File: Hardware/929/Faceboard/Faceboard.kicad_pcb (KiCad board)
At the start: 4 copper layers, 154 x 144 mm, 94 parts, among them J2 Raspberry_Pi_to_Ziloo, J3 Debug_4-2328724-5, P1 UCM-P1, P2 UCM-P2, P5 T-USB_PWRCTL-50, P6 T-USB_HIGH-SPEED-50, P7 202-SMART-CAM, Q1 2SC4213, U10 CBTL04083ABS_518, U11 TS5USBC410YFFR, U12 FR2032, U16 TXS0104, U16 YZT12, U17 TXS0104, U17 YZT12, U18 SN74CB3Q3245RGYR, U19 TXS0104, U20 TXS0104, U21 TXS0104, U3 SN74CB3Q3245RGYR, U6 Supervisor M2, U7 TCA9534, Y1 25.000MHz

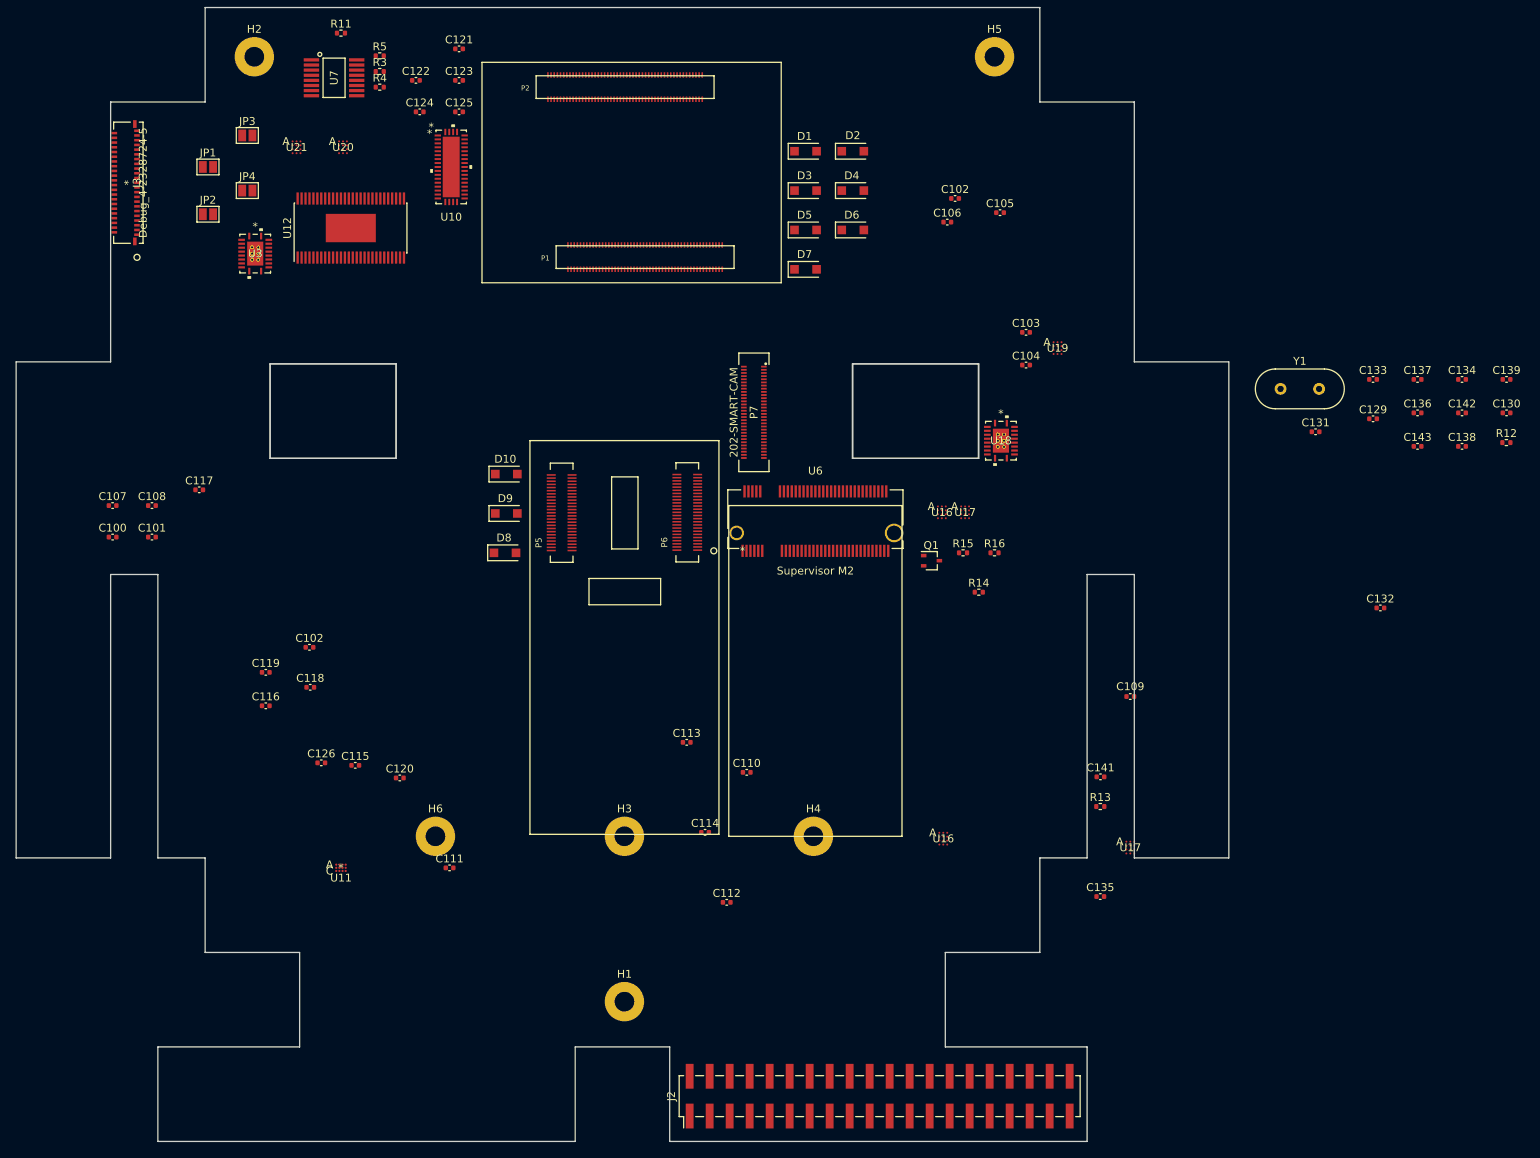
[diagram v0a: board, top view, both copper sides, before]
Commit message: Added components
ESD HDMI
Extra components planned
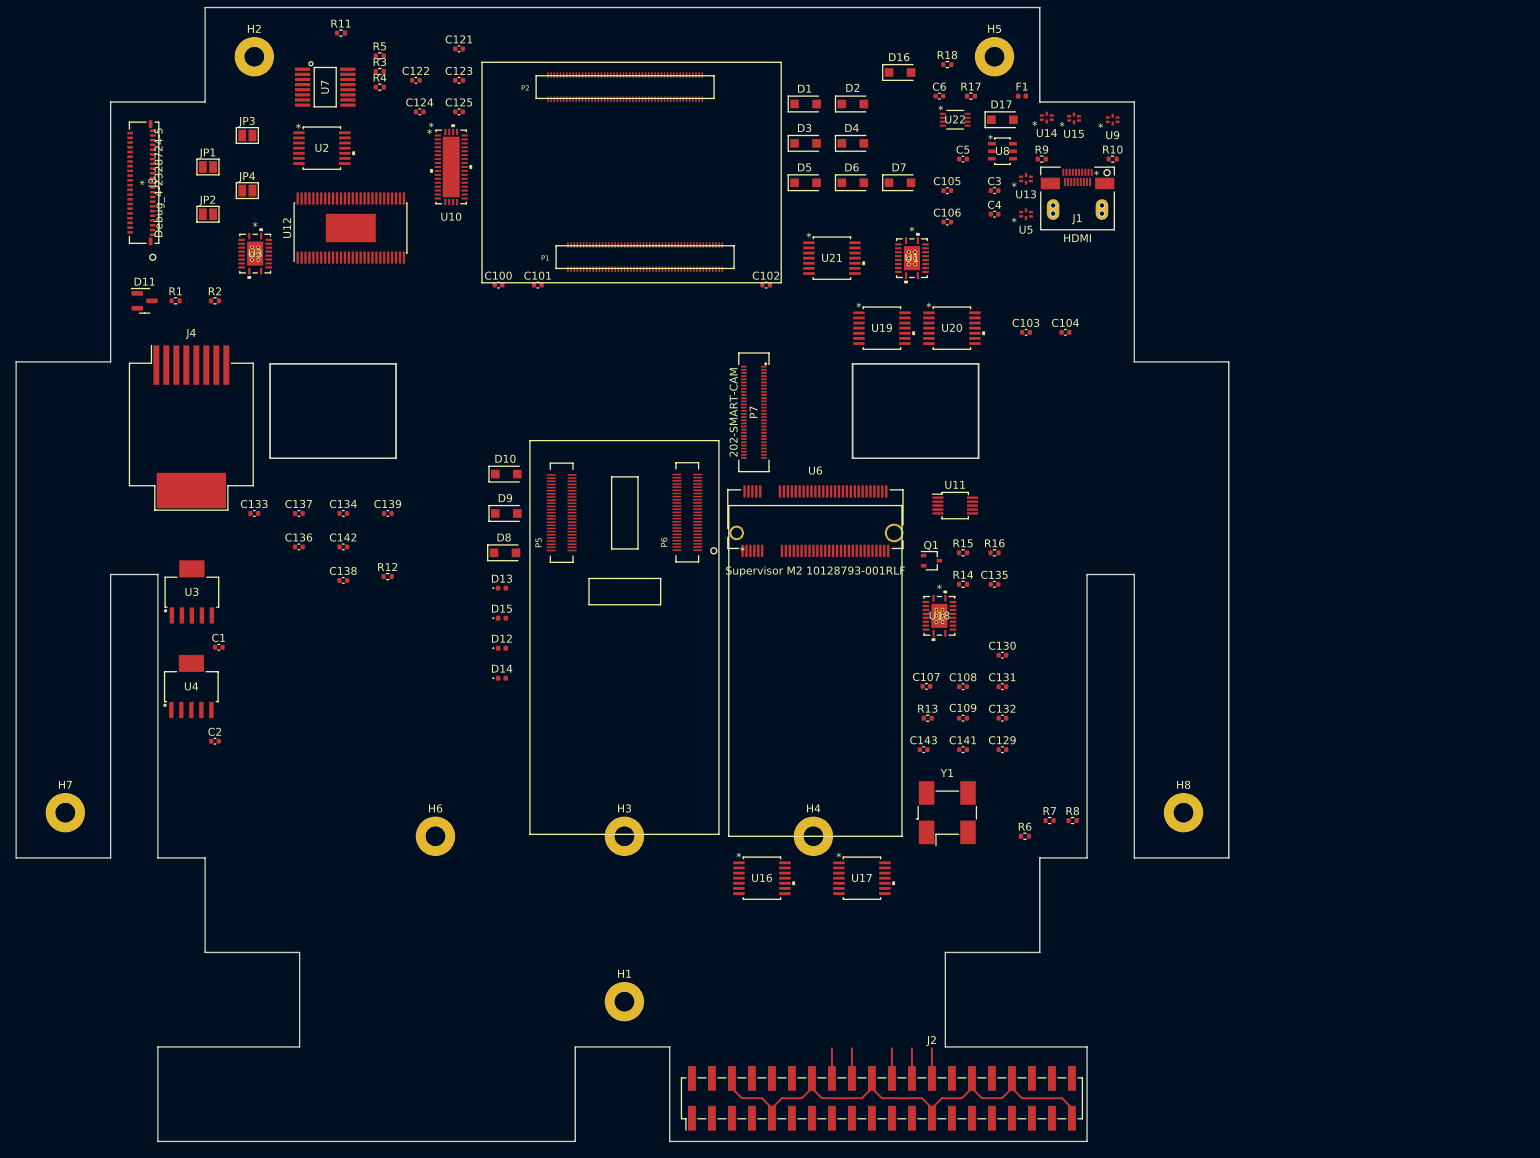
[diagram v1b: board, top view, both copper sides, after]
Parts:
- removed the C102 at (149.2, 61.2)
- removed C110, C111, C112, C113, C114, C115, C117, C118, C119, C120: 100nF, Capacitor_SMD:C_0402_1005Metric
- removed C116: 1uF, Capacitor_SMD:C_0402_1005Metric
- removed C126: CAP, Capacitor_SMD:C_0402_1005Metric
- removed the U16 at (147.7, 142.5)
- removed the U16 at (147.6, 101.1)
- removed the U17 at (150.5, 101.1)
- removed the U17 at (171.5, 143.7)
- added C1: C, Capacitor_SMD:C_0402_1005Metric, F.Cu at (55.7, 118.2)
- added C2: C, Capacitor_SMD:C_0402_1005Metric, F.Cu at (55.2, 130.2)
- added C3: 1uF, Capacitor_SMD:C_0402_1005Metric, F.Cu at (154.2, 60.2)
- added C4: 1uF, Capacitor_SMD:C_0402_1005Metric, F.Cu at (154.2, 63.2)
- added C5: 1uF, Capacitor_SMD:C_0402_1005Metric, F.Cu at (150.2, 56.2)
- added C6: 10nF, Capacitor_SMD:C_0402_1005Metric, F.Cu at (147.2, 48.2)
- added D11: BAT54C, Package_TO_SOT_SMD:SOT-23, F.Cu at (46.3, 74.2)
- added D12: D, Diode_SMD:D_0402_1005Metric, F.Cu at (91.7, 118.4)
- added D13: D, Diode_SMD:D_0402_1005Metric, F.Cu at (91.7, 110.7)
- added D14: D, Diode_SMD:D_0402_1005Metric, F.Cu at (91.7, 122.2)
- added D15: D, Diode_SMD:D_0402_1005Metric, F.Cu at (91.7, 114.5)
- added D16: 1A Schottky, Diode_SMD:D_SOD-123F, F.Cu at (142.2, 45.2)
- added D17: 1A Schottky, Diode_SMD:D_SOD-123F, F.Cu at (155.2, 51.2)
- added F1: Polyfuse_Small, Fuse:Fuse_0402_1005Metric, F.Cu at (157.7, 48.2)
- added H7: MountingHole, MountingHole:MountingHole_2.5mm_Pad, F.Cu at (36.2, 139.2)
- added H8: MountingHole, MountingHole:MountingHole_2.5mm_Pad, F.Cu at (178.2, 139.2)
- added J1: HDMI, Ziloo:467652301, F.Cu at (164.8, 61.2)
- added J4: RJ45_LED_Shielded, Connector_RJ:RJ45_Molex_0855135013_Vertical, F.Cu at (52.2, 90.2)
- added R1: 475Ohm, Resistor_SMD:R_0402_1005Metric, F.Cu at (50.2, 74.2)
- added R10: 1K2, Resistor_SMD:R_0402_1005Metric, F.Cu at (169.2, 56.2)
- added R17: 1K/1%, Resistor_SMD:R_0402_1005Metric, F.Cu at (151.2, 48.2)
- added R18: 200K, Resistor_SMD:R_0402_1005Metric, F.Cu at (148.2, 44.2)
- added R2: 475Ohm, Resistor_SMD:R_0402_1005Metric, F.Cu at (55.2, 74.2)
- added R6: 2M, Resistor_SMD:R_0402_1005Metric, F.Cu at (158.1, 142.2)
- added R7: 1M, Resistor_SMD:R_0402_1005Metric, F.Cu at (161.2, 140.2)
- added R8: 1K, Resistor_SMD:R_0402_1005Metric, F.Cu at (164.2, 140.2)
- added R9: 47K, Resistor_SMD:R_0402_1005Metric, F.Cu at (160.2, 56.2)
- added U1: SN74CB3Q3245RGYR, Ziloo:SN74CB3Q3245RGYR, F.Cu at (143.8, 68.8)
- added U13: LCFE121002H900TG, Ziloo:LCFE121002H900TG, F.Cu at (158.2, 58.8)
- added U14: LCFE121002H900TG, Ziloo:LCFE121002H900TG, F.Cu at (160.9, 51.0)
- added U15: LCFE121002H900TG, Ziloo:LCFE121002H900TG, F.Cu at (164.3, 51.1)
- added U16: TXS0104EPWR, Ziloo:TXS0104EPWR, F.Cu at (124.7, 147.6)
- added U17: TXS0104EPWR, Ziloo:TXS0104EPWR, F.Cu at (137.4, 147.6)
- added U2: SN74CBTLV3126PWR, Ziloo:SN74CBTLV3126PWR, F.Cu at (68.8, 54.9)
- added U22: PCA9306DCUR, Ziloo:PCA9306DCUR, F.Cu at (149.2, 51.2)
- added U3: TPS79633DCQ, Ziloo:TPS79633DCQ, F.Cu at (52.3, 111.2)
- added U4: TPS79618DCQR, Ziloo:TPS79618DCQR, F.Cu at (52.2, 123.2)
- added U5: LCFE121002H900TG, Ziloo:LCFE121002H900TG, F.Cu at (158.2, 63.2)
- added U8: IP4220CZ6, Ziloo:IP4220CZ6, F.Cu at (155.2, 55.2)
- added U9: LCFE121002H900TG, Ziloo:LCFE121002H900TG, F.Cu at (169.2, 51.2)
- P5: value T-USB_PWRCTL-50 -> 292_PWRCTL-50
- P6: value T-USB_HIGH-SPEED-50 -> 292_HIGH-SPEED-50
- U11: value TS5USBC410YFFR -> FSUSB42MUX; footprint Ziloo:TS5USBC410YFFR -> Package_SO:MSOP-10_3x3mm_P0.5mm
- U12: value FR2032 -> Faceboard_Expander_FR2032IG56
- U19, U20, U21: value TXS0104 -> TXS0104EPWR; footprint Ziloo:TXS0104EYZTR -> Ziloo:TXS0104EPWR
- U6: value Supervisor M2 -> Supervisor M2 10128793-001RLF
- Y1: footprint Crystal:Crystal_HC18-U_Vertical -> Oscillator:Oscillator_SMD_Abracon_ASV-4Pin_7.0x5.1mm_HandSoldering
- moved C133 143.1 mm to (60.2, 101.2)
- moved C134 143.1 mm to (71.5, 101.2)
- moved C136 143.1 mm to (65.9, 105.5)
- moved C137 143.1 mm to (65.9, 101.2)
- moved C138 143.1 mm to (71.5, 109.8)
- moved C139 143.1 mm to (77.2, 101.2)
- moved C142 143.1 mm to (71.5, 105.5)
- moved R12 143.1 mm to (77.2, 109.3)
- moved C107 105.9 mm to (145.6, 123.2)
- moved C108 105.5 mm to (150.2, 123.2)
- moved U11 90.6 mm to (149.2, 100.2)
- moved U20 80.7 mm to (148.8, 77.7)
- moved C102 74.0 mm to (125.2, 72.2)
- moved C143 73.6 mm to (145.2, 131.2)
- moved C130 71.0 mm to (155.2, 119.2)
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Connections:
- net /Expander, M.2 and T-USB/M.2 Key B connector/B_PWROFF renamed Net-(R13-Pad1)
- net /Expander, M.2 and T-USB/SPI2_SS0 renamed /Expander, M.2 and T-USB/POWER_TO_SYS_STEM
- net /UART1_TXD renamed /C_EX_RXD
- net Net-(D6-Pad2) renamed /Expander, M.2 and T-USB/VSOM
- C103 pad 1: +1V8 -> SLEEP_1V8
- C104 pad 1: +3.3V -> CAM_3V3
- C105 pad 1: +1V8 -> SLEEP_1V8
- C106 pad 1: +3.3V -> CAM_3V3
- C107 pad 1: +1V8 -> SLEEP_1V8
- C108 pad 1: +3.3V -> CAM_3V3
- C121 pad 2: +3.3V -> LIVE_3V3
- C122 pad 2: +3.3V -> LIVE_3V3
- C123 pad 2: +3.3V -> LIVE_3V3
- C124 pad 2: +3.3V -> LIVE_3V3
- C125 pad 2: +3.3V -> LIVE_3V3
- C130 pad 1: +3.3V -> LIVE_3V3
- C131 pad 1: +3.3V -> LIVE_3V3
- C132 pad 1: +3.3V -> LIVE_3V3
- C133 pad 1: +1V8 -> LIVE_1V8
- C134 pad 1: +3.3V -> LIVE_3V3
- C136 pad 1: +3.3V -> LIVE_3V3
- C137 pad 1: +3.3V -> LIVE_3V3
- C138 pad 1: +3.3V -> LIVE_3V3
- C139 pad 1: +3.3V -> LIVE_3V3
- C141 pad 1: +1V8 -> LIVE_1V8
- C142 pad 1: +3.3V -> LIVE_3V3
- D8 pad 2: Net-(D8-Pad2) -> Net-(P5-Pad15)
- J2 pad 1: unconnected-(J2-Pad1) -> LIVE_3V3
- J2 pad 13: unconnected-(J2-Pad13) -> /Ethernet and SD1/SD1_DATA3
- J2 pad 14: unconnected-(J2-Pad14) -> GND
- J2 pad 15: unconnected-(J2-Pad15) -> /Ethernet and SD1/SD1_CLK
- J2 pad 16: unconnected-(J2-Pad16) -> /Ethernet and SD1/SD1_CMD
- J2 pad 17: unconnected-(J2-Pad17) -> LIVE_3V3
- J2 pad 18: unconnected-(J2-Pad18) -> /Ethernet and SD1/SD1_DATA0
- J2 pad 2: unconnected-(J2-Pad2) -> HDMI_5V
- J2 pad 20: unconnected-(J2-Pad20) -> GND
- J2 pad 22: unconnected-(J2-Pad22) -> /Ethernet and SD1/SD1_DATA1
- J2 pad 25: unconnected-(J2-Pad25) -> GND
- J2 pad 27: unconnected-(J2-Pad27) -> /Ethernet and SD1/SYS_I2C_SDA
- J2 pad 28: unconnected-(J2-Pad28) -> /Ethernet and SD1/SYS_I2C_SCL
- J2 pad 3: unconnected-(J2-Pad3) -> /Ethernet and SD1/STEM_I2C_SDA
- J2 pad 30: unconnected-(J2-Pad30) -> GND
- J2 pad 34: unconnected-(J2-Pad34) -> GND
- J2 pad 37: unconnected-(J2-Pad37) -> /Ethernet and SD1/SD1_DATA2
- J2 pad 39: unconnected-(J2-Pad39) -> GND
- J2 pad 4: unconnected-(J2-Pad4) -> HDMI_5V
- J2 pad 5: unconnected-(J2-Pad5) -> /Ethernet and SD1/STEM_I2C_SCL
- J2 pad 6: unconnected-(J2-Pad6) -> GND
- J2 pad 7: unconnected-(J2-Pad7) -> /Ethernet and SD1/STEM_INT
- J2 pad 9: unconnected-(J2-Pad9) -> GND
- J3 pad 14: unconnected-(J3-Pad14) -> /Expander, M.2 and T-USB/SJTAG_MOD
- J3 pad 2: +3.3V -> CAM_3V3
- J3 pad 24: unconnected-(J3-Pad24) -> Net-(J3-Pad24)
- J3 pad 25: unconnected-(J3-Pad25) -> Net-(J3-Pad25)
- J3 pad 26: unconnected-(J3-Pad26) -> Net-(J3-Pad26)
- J3 pad 27: unconnected-(J3-Pad27) -> Net-(J3-Pad27)
- J3 pad 28: unconnected-(J3-Pad28) -> Net-(J3-Pad28)
- J3 pad 29: unconnected-(J3-Pad29) -> Net-(J3-Pad29)
- J3 pad 5: unconnected-(J3-Pad5) -> /Expander, M.2 and T-USB/UART2_RXD
- J3 pad 6: unconnected-(J3-Pad6) -> /Expander, M.2 and T-USB/UART2_RXD
- J3 pad 8: unconnected-(J3-Pad8) -> /Expander, M.2 and T-USB/UART4_RXD
- J3 pad 9: unconnected-(J3-Pad9) -> /Expander, M.2 and T-USB/UART4_TXD
- JP2 pad 1: unconnected-(JP2-Pad1) -> /Expander, M.2 and T-USB/SYS_PD_CTL_INT
- JP3 pad 1: /Expander, M.2 and T-USB/SYS_I2C_SDA -> /Expander, M.2 and T-USB/POWER_PD_CTL_INT
- JP4 pad 1: /Expander, M.2 and T-USB/SYS_I2C_SCL -> /Expander, M.2 and T-USB/BAT_INT
- P1 pad 87: /NIGHT_I2C_SCL -> /I2C6_SCL
- P1 pad 89: /NIGHT_I2C_SDA -> /I2C6_SDA
- P5 pad 10: unconnected-(P5-Pad10) -> Net-(J3-Pad29)
- P5 pad 11: /Expander, M.2 and T-USB/BOTH_VSOM -> GND
- P5 pad 15: Net-(D8-Pad2) -> Net-(P5-Pad15)
- P5 pad 16: /Expander, M.2 and T-USB/SYS_RST_PMIC -> /Expander, M.2 and T-USB/USB_XD_OE
- P5 pad 17: /Expander, M.2 and T-USB/POR_B_3P3 -> /Expander, M.2 and T-USB/USB_XD_SEL
- P5 pad 20: /Expander, M.2 and T-USB/VCC_RTC -> /Expander, M.2 and T-USB/ALT_BOOT
- P5 pad 22: /Expander, M.2 and T-USB/ALT_BOOT -> unconnected-(P5-Pad22)
- P5 pad 23: unconnected-(P5-Pad23) -> /Expander, M.2 and T-USB/BAT_INT
- P5 pad 24: unconnected-(P5-Pad24) -> /Expander, M.2 and T-USB/BAT_CE
- P5 pad 25: unconnected-(P5-Pad25) -> /Expander, M.2 and T-USB/BAT_EN
- P5 pad 27: unconnected-(P5-Pad27) -> /Expander, M.2 and T-USB/SHUTDOWN_BTN
- P5 pad 28: unconnected-(P5-Pad28) -> /Expander, M.2 and T-USB/LOCK_BTN
- P5 pad 35: /Expander, M.2 and T-USB/NIGHT_I2C_SDA -> /Expander, M.2 and T-USB/POWER_SDA
- P5 pad 36: /Expander, M.2 and T-USB/NIGHT_I2C_SCL -> /Expander, M.2 and T-USB/POWER_SCL
- P5 pad 40: unconnected-(P5-Pad40) -> CAM_3V3
- P5 pad 41: /Expander, M.2 and T-USB/UART4_TXD -> unconnected-(P5-Pad41)
- P5 pad 42: /Expander, M.2 and T-USB/UART4_RXD -> unconnected-(P5-Pad42)
- P5 pad 43: /Expander, M.2 and T-USB/UART3_RXD -> CAM_3V3
- P5 pad 44: /Expander, M.2 and T-USB/UART3_TXD -> Net-(J3-Pad27)
- P5 pad 45: /Expander, M.2 and T-USB/UART2_RXD -> Net-(J3-Pad26)
- P5 pad 46: /Expander, M.2 and T-USB/UART2_RXD -> HDMI_5V
- P5 pad 47: /Expander, M.2 and T-USB/FACE-EX_FW_RXD -> Net-(J3-Pad25)
- P5 pad 48: /Expander, M.2 and T-USB/UART1_TXD -> Net-(J3-Pad24)
- P5 pad 49: GND -> /Expander, M.2 and T-USB/VCC_RTC
- P5 pad 9: unconnected-(P5-Pad9) -> Net-(J3-Pad28)
- P6 pad 19: /Expander, M.2 and T-USB/FACE-EX_FW_TXD -> /Expander, M.2 and T-USB/STEM_INT
- P6 pad 21: /Expander, M.2 and T-USB/T_SBWTCK -> unconnected-(P6-Pad21)
- P6 pad 23: /Expander, M.2 and T-USB/T_SBWTDIO -> unconnected-(P6-Pad23)
- P6 pad 27: /Expander, M.2 and T-USB/T-USB-EX_FW_TXD -> unconnected-(P6-Pad27)
- P6 pad 28: /Expander, M.2 and T-USB/T-USB-EX_FW_RXD -> unconnected-(P6-Pad28)
- P6 pad 30: unconnected-(P6-Pad30) -> /Expander, M.2 and T-USB/PWR_CHARGE
- P7 pad 12: +1V8 -> SLEEP_1V8
- P7 pad 24: +3.3V -> CAM_3V3
- P7 pad 30: +1V8 -> SLEEP_1V8
- P7 pad 35: unconnected-(P7-Pad35) -> /Camera + Sound Domain/C_FW_TXD
- P7 pad 37: unconnected-(P7-Pad37) -> /Camera + Sound Domain/C_FW_RXD
- P7 pad 47: unconnected-(P7-Pad47) -> /Camera + Sound Domain/SD_CS_SOM
- P7 pad 49: unconnected-(P7-Pad49) -> /Camera + Sound Domain/SD_D3
- P7 pad 51: unconnected-(P7-Pad51) -> /Camera + Sound Domain/SD_D2
- P7 pad 53: unconnected-(P7-Pad53) -> /Camera + Sound Domain/SD_D1
- P7 pad 55: unconnected-(P7-Pad55) -> /Camera + Sound Domain/SD_D0
- P7 pad 57: unconnected-(P7-Pad57) -> /Camera + Sound Domain/SD_CLK
- P7 pad 59: unconnected-(P7-Pad59) -> /Camera + Sound Domain/SD_CMD
- P7 pad 6: +3.3V -> CAM_3V3
- R11 pad 1: +3.3V -> LIVE_3V3
- R12 pad 2: +3.3V -> LIVE_3V3
- R13 pad 2: +3.3V -> LIVE_3V3
- R14 pad 1: +3.3V -> LIVE_3V3
- R3 pad 1: +3.3V -> LIVE_3V3
- R4 pad 1: Net-(R4-Pad1) -> Net-(U7-Pad1)
- R5 pad 1: +3.3V -> LIVE_3V3
- R5 pad 2: Net-(R5-Pad2) -> Net-(U7-Pad2)
- U10 pad 13: +3.3V -> LIVE_3V3
- U10 pad 18: +3.3V -> LIVE_3V3
- U10 pad 20: +3.3V -> LIVE_3V3
- U10 pad 30: +3.3V -> LIVE_3V3
- U10 pad 40: +3.3V -> LIVE_3V3
- U10 pad 42: +3.3V -> LIVE_3V3
- U10 pad 5: +3.3V -> LIVE_3V3
- U10 pad 8: +3.3V -> LIVE_3V3
- U12 pad 12: unconnected-(U12-Pad12) -> /Expander, M.2 and T-USB/STEM_INT
- U12 pad 13: unconnected-(U12-Pad13) -> /Expander, M.2 and T-USB/MCU_SYS_INT
- U12 pad 16: /Expander, M.2 and T-USB/F_SBWTDIO -> /Expander, M.2 and T-USB/FACE_RST
- U12 pad 17: /Expander, M.2 and T-USB/F_SBWTCK -> /Expander, M.2 and T-USB/FACE_SBWTCK
- U12 pad 18: Net-(D10-Pad2) -> /Expander, M.2 and T-USB/PD_USBC_INT
- U12 pad 19: Net-(D8-Pad2) -> /Expander, M.2 and T-USB/POWER_TO_STEM
- U12 pad 20: unconnected-(U12-Pad20) -> /Expander, M.2 and T-USB/POWER_TO_SYS
- U12 pad 25: /Expander, M.2 and T-USB/MCU_SYS_INT -> /Expander, M.2 and T-USB/VSOM_LESS_1V4
- U12 pad 26: /Expander, M.2 and T-USB/UART1_TXD -> /Expander, M.2 and T-USB/PWR_CHARGE_LESS_1V4
- U12 pad 27: /Expander, M.2 and T-USB/FACE-EX_FW_RXD -> /Expander, M.2 and T-USB/FACE_FW_RXD
- U12 pad 28: /Expander, M.2 and T-USB/FACE-EX_FW_TXD -> /Expander, M.2 and T-USB/FACE_FW_TXD
- U12 pad 33: unconnected-(U12-Pad33) -> /Expander, M.2 and T-USB/SYS_I2C_SCL
- U12 pad 34: unconnected-(U12-Pad34) -> /Expander, M.2 and T-USB/SYS_I2C_SDA
- U12 pad 35: unconnected-(U12-Pad35) -> /Expander, M.2 and T-USB/PD_HRESET
- U12 pad 38: /Expander, M.2 and T-USB/SD2_nCD -> /Expander, M.2 and T-USB/BAT_EN
- U12 pad 39: /Expander, M.2 and T-USB/BOTH_VSOM -> /Expander, M.2 and T-USB/BAT_CE
- U12 pad 4: unconnected-(U12-Pad4) -> /Expander, M.2 and T-USB/POWER_SDA
- U12 pad 5: unconnected-(U12-Pad5) -> /Expander, M.2 and T-USB/POWER_SCL
- U12 pad 51: unconnected-(U12-Pad51) -> /Expander, M.2 and T-USB/USB_XD_SEL
- U12 pad 52: unconnected-(U12-Pad52) -> /Expander, M.2 and T-USB/USB_XD_OE
- U12 pad 8: unconnected-(U12-Pad8) -> /Expander, M.2 and T-USB/SHUTDOWN_BTN
- U12 pad 9: unconnected-(U12-Pad9) -> /Expander, M.2 and T-USB/LOCK_BTN
- U18 pad 20: +3.3V -> LIVE_3V3
- U3 pad 20: +3.3V -> CAM_3V3
- U6 pad 2: +3.3V -> LIVE_3V3
- U6 pad 70: +3.3V -> LIVE_3V3
- U6 pad 72: +3.3V -> LIVE_3V3
- U6 pad 74: +3.3V -> LIVE_3V3
- U7 pad 1: Net-(R5-Pad2) -> Net-(U7-Pad1)
- U7 pad 16: +3.3V -> LIVE_3V3
- U7 pad 2: Net-(R4-Pad1) -> Net-(U7-Pad2)
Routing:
- net GND: track 0.00 -> 60.6 mm
- net unconnected-(J2-Pad26): track 0.00 -> 3.84 mm
- net unconnected-(J2-Pad24): track 0.00 -> 3.84 mm
- net /Ethernet and SD1/SD1_DATA1: track 0.00 -> 3.84 mm
- net /Ethernet and SD1/SD1_DATA0: track 0.00 -> 3.84 mm
- net /Ethernet and SD1/SD1_CMD: track 0.00 -> 3.84 mm

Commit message: Removed VSOM diodes
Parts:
- removed D1, D10, D2, D3, D4, D5, D6, D7, D8, D9: D_Schottky, Diode_SMD:D_SOD-123F
- removed R6: 2M, Resistor_SMD:R_0402_1005Metric
- removed R7: 1M, Resistor_SMD:R_0402_1005Metric
- removed R8: 1K, Resistor_SMD:R_0402_1005Metric
- added D11: BAT54C, Package_TO_SOT_SMD:SOT-23, F.Cu at (60.2, 76.2)
- added D18: LED, LED_SMD:LED_0805_2012Metric, F.Cu at (50.8, 104.2)
- added D19: LED, LED_SMD:LED_0805_2012Metric, F.Cu at (55.2, 104.2)
- added GPIO**: Front Face GPIO HEader, Connector_PinHeader_2.54mm:PinHeader_2x20_P2.54mm_Vertical_SMD, B.Cu at (108.2, 52.7)
- J4: value RJ45_LED_Shielded -> RJ45
- moved J3 119.8 mm to (162.4, 88.8)
- moved C102 14.2 mm to (136.2, 63.2)
- moved C101 11.0 mm to (85.2, 72.2)
- moved C100 7.21 mm to (85.2, 68.2)
- moved P1 3.01 mm to (109.8, 71.7)
- moved P2 3.01 mm to (107.3, 50.1)
- moved J4 1.01 mm to (53.2, 90.4)
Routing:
- net (no net): track 0.00 -> 1574.7 mm, vias 0 -> 114
- net +VDC: track 0.00 -> 112.9 mm
- net /HDMI_DDC_SCL: track 0.00 -> 18.6 mm
- net unconnected-(U10-Pad22): track 0.00 -> 10.3 mm, vias 0 -> 1
- net CAM_3V3: track 0.00 -> 8.91 mm
- net Net-(C102-Pad2): track 0.00 -> 8.67 mm
- net /UART1_RXD: track 0.00 -> 7.42 mm
- net /I2C5_SDA: track 0.00 -> 7.42 mm
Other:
- outline, holes or cut-outs redrawn
- board text added: "JLCJLCJLCJLC"

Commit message: PoC board task
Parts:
- removed C1: C, Capacitor_SMD:C_0402_1005Metric
- removed the U3 at (52.3, 111.2)
- added J5: UCM-P20-misc, Connector_PinHeader_2.54mm:PinHeader_2x17_P2.54mm_Vertical_SMD, F.Cu at (71.5, 128.5)
- added J6: UCM-P21-misc, Connector_PinHeader_2.54mm:PinHeader_2x17_P2.54mm_Vertical_SMD, F.Cu at (78.1, 175.1)
- added J7: USB_B_Micro, Connector_USB:USB_Micro-B_Wuerth_629105150521, F.Cu at (178.1, 109.0)
- added P4: Power, Connector_PinHeader_2.54mm:PinHeader_2x06_P2.54mm_Vertical_SMD, F.Cu at (131.2, 160.5)
- added R19: 0R, Resistor_SMD:R_0402_1005Metric, F.Cu at (181.6, 90.2)
- added R20: 0R, Resistor_SMD:R_0402_1005Metric, F.Cu at (49.4, 65.1)
- added R21: 0R, Resistor_SMD:R_0402_1005Metric, F.Cu at (181.6, 93.8)
- added R22: 0R, Resistor_SMD:R_0402_1005Metric, F.Cu at (49.4, 68.8)
- added R6: 0R, Resistor_SMD:R_0402_1005Metric, F.Cu at (49.5, 51.9)
- added R7: DNP, Resistor_SMD:R_0402_1005Metric, F.Cu at (49.3, 55.9)
- added R8: 0R, Resistor_SMD:R_0402_1005Metric, F.Cu at (49.1, 59.3)
- added SW1: Reset, Button_Switch_SMD:SW_SPST_EVQP7A, F.Cu at (44.3, 54.1)
- added SW2: Power, Button_Switch_SMD:SW_SPST_EVQP7A, F.Cu at (181.7, 99.1)
- added SW3: Alt. Boot, Button_Switch_SMD:SW_SPST_EVQP7A, F.Cu at (44.3, 66.4)
- added SW4: Power, Connector_PinHeader_2.54mm:PinHeader_2x06_P2.54mm_Vertical_SMD, F.Cu at (131.1, 124.2)
- added U23: SN74CB3Q3245RGYR, Ziloo:SN74CB3Q3245RGYR, F.Cu at (151.5, 150.7)
- moved C2 46.6 mm to (91.6, 101.0)
- moved U4 36.8 mm to (83.6, 103.9)
- moved H8 32.2 mm to (161.8, 111.6)
- moved H7 31.3 mm to (52.3, 112.4)
- moved D14 4.83 mm to (91.9, 117.3)
- moved D12 4.83 mm to (91.9, 113.5)
- moved D13 4.83 mm to (91.9, 105.9)
- moved D15 4.83 mm to (91.9, 109.7)
- moved H3 2.00 mm to (107.2, 144.2)
- moved H4 2.00 mm to (131.2, 144.2)
- moved H6 2.00 mm to (83.2, 144.2)
- moved P5 2.00 mm to (99.3, 103.2)
- moved P6 2.00 mm to (115.2, 103.1)
- moved U16 2.00 mm to (124.7, 149.6)
- moved U17 2.00 mm to (137.4, 149.6)
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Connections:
- net /Camera + Sound Domain/RIGHT_SCL renamed /Camera + Sound Domain/C_SBWTCK
- net /Camera + Sound Domain/RIGHT_SDA renamed /Camera + Sound Domain/C_SBWTDIO
- net /Camera + Sound Domain/STEM_INT renamed /Camera + Sound Domain/STEM_MSG
- net /Expander, M.2 and T-USB/LEFT_PWRDN renamed /Expander, M.2 and T-USB/CAM_SBWTDIO
- net /Expander, M.2 and T-USB/LEFT_RESET renamed /Expander, M.2 and T-USB/CAM_SBWTCK
- net /Expander, M.2 and T-USB/RIGHT_ATT_XSHUT renamed /Expander, M.2 and T-USB/FACE2_SBWTDIO
- net /Expander, M.2 and T-USB/UART4_RXD renamed /Expander, M.2 and T-USB/COREM_TXD
- net /Expander, M.2 and T-USB/UART4_TXD renamed /Expander, M.2 and T-USB/COREM_RXD
- net /M2_PCIE_CLKREQ renamed /PCIE_CLKREQ
- net /SAI5_TX_DATA1 renamed /SAI5_TXD1
- net /SD2_DATA0 renamed /SD2_D0
- net /SD2_DATA1 renamed /SD2_D1
- net /SD_CLK renamed /SD2_CLK
- net /SD_CMD renamed /SD2_CMD
- net /SD_CS_SOM renamed /SD2_CS_SOM
- net /SD_D2 renamed /SD2_D2
- net /SD_D3 renamed /SD2_D3
- net /STEM_INT renamed /GPIO1_IO1
- net Net-(J3-Pad28) renamed /Expander, M.2 and T-USB/SBU1
- net Net-(J3-Pad29) renamed /Expander, M.2 and T-USB/SBU2
- net SLEEP_1V8 renamed CAM_1V8
- C104 pad 1: CAM_3V3 -> SLEEP_3V3
- C106 pad 1: CAM_3V3 -> SLEEP_3V3
- C108 pad 1: CAM_3V3 -> SLEEP_3V3
- D13 pad 1: /Expander, M.2 and T-USB/VSOM -> VSOM
- J2 pad 1: LIVE_3V3 -> /Ethernet and SD1/RPI_3V3
- J2 pad 10: unconnected-(J2-Pad10) -> Net-(J2-Pad10)
- J2 pad 17: LIVE_3V3 -> /Ethernet and SD1/RPI_3V3
- J2 pad 2: HDMI_5V -> /Ethernet and SD1/RPI_5V
- J2 pad 32: unconnected-(J2-Pad32) -> Net-(J2-Pad32)
- J2 pad 33: unconnected-(J2-Pad33) -> Net-(J2-Pad33)
- J2 pad 4: HDMI_5V -> /Ethernet and SD1/RPI_5V
- J2 pad 8: unconnected-(J2-Pad8) -> Net-(J2-Pad8)
- J3 pad 1: unconnected-(J3-Pad1) -> /Expander, M.2 and T-USB/SPI2_CLK
- J3 pad 11: /Expander, M.2 and T-USB/SJTAG_TDI -> /Expander, M.2 and T-USB/FACE_TCK
- J3 pad 12: /Expander, M.2 and T-USB/SJTAG_TMS -> /Expander, M.2 and T-USB/FACE_TMS
- J3 pad 13: /Expander, M.2 and T-USB/SJTAG_TCK -> /Expander, M.2 and T-USB/FACE_TDI
- J3 pad 14: /Expander, M.2 and T-USB/SJTAG_MOD -> /Expander, M.2 and T-USB/FACE_TDO
- J3 pad 15: /Expander, M.2 and T-USB/SJTAG_TDO -> /Expander, M.2 and T-USB/FACE_RST
- J3 pad 16: /Expander, M.2 and T-USB/SYS_RST_PMIC -> SLEEP_3V3
- J3 pad 18: unconnected-(J3-Pad18) -> /Expander, M.2 and T-USB/SYS_RST_PMIC
- J3 pad 2: CAM_3V3 -> /Expander, M.2 and T-USB/SPI2_MISO
- J3 pad 20: unconnected-(J3-Pad20) -> SLEEP_3V3
- J3 pad 23: unconnected-(J3-Pad23) -> /Expander, M.2 and T-USB/PD_HRESET
- J3 pad 3: unconnected-(J3-Pad3) -> /Expander, M.2 and T-USB/SPI2_MOSI
- J3 pad 30: unconnected-(J3-Pad30) -> /Expander, M.2 and T-USB/FACE_SBWTCK
- J3 pad 31: unconnected-(J3-Pad31) -> /Expander, M.2 and T-USB/FACE_RST
- J3 pad 32: unconnected-(J3-Pad32) -> /Expander, M.2 and T-USB/FACE_FW_TXD
- J3 pad 33: /Expander, M.2 and T-USB/LEFT_ATT_XSHUT -> /Expander, M.2 and T-USB/FACE_FW_RXD
- J3 pad 36: unconnected-(J3-Pad36) -> /Expander, M.2 and T-USB/CAM_FW_RXD
- J3 pad 37: unconnected-(J3-Pad37) -> /Expander, M.2 and T-USB/CAM_FW_TXD
- J3 pad 38: unconnected-(J3-Pad38) -> /Expander, M.2 and T-USB/FACE2_SBWTCK
- J3 pad 4: GND -> /Expander, M.2 and T-USB/T-USB_SPI_CS
- J3 pad 40: /Expander, M.2 and T-USB/RIGHT_RESET -> /Expander, M.2 and T-USB/POWER_SCL
- J3 pad 41: /Expander, M.2 and T-USB/RIGHT_PWRDN -> /Expander, M.2 and T-USB/POWER_SDA
- J3 pad 5: /Expander, M.2 and T-USB/UART2_RXD -> /Expander, M.2 and T-USB/FLASH_HOLD
- J3 pad 6: /Expander, M.2 and T-USB/UART2_RXD -> unconnected-(J3-Pad6)
- P1 pad 11: +VDC -> VSOM
- P1 pad 21: /UART1_RXD -> /UART3_RXD
- P1 pad 27: +VDC -> VSOM
- P1 pad 43: +VDC -> VSOM
- P1 pad 49: unconnected-(P1-Pad49) -> /CAN2_RX
- P1 pad 57: +VDC -> VSOM
- P1 pad 61: /C_EX_RXD -> /UART3_TXD
- P1 pad 69: +VDC -> VSOM
- P1 pad 72: /C_EX_RXD -> /UART1_TXD
- P1 pad 74: /C_EX_RXD -> /F_EX_RXD
- P1 pad 76: /UART1_RXD -> /F_EX_TXD
- P1 pad 83: +VDC -> VSOM
- P1 pad 84: /UART1_RXD -> /C_EX_TXD
- P1 pad 93: /VCC_RTC -> SLEEP_3V3
- P2 pad 19: +VDC -> VSOM
- P2 pad 29: +VDC -> VSOM
- P2 pad 39: +VDC -> VSOM
- P2 pad 57: +VDC -> VSOM
- P2 pad 71: +VDC -> VSOM
- P2 pad 87: +VDC -> VSOM
- P2 pad 9: +VDC -> VSOM
- P5 pad 1: Net-(D9-Pad2) -> /Expander, M.2 and T-USB/VSOM_TU
- P5 pad 15: Net-(P5-Pad15) -> /Expander, M.2 and T-USB/VSOM_TU
- P5 pad 18: /Expander, M.2 and T-USB/PMIC_ON_REQ -> unconnected-(P5-Pad18)
- P5 pad 19: /Expander, M.2 and T-USB/PMIC_STBY_REQ -> unconnected-(P5-Pad19)
- P5 pad 20: /Expander, M.2 and T-USB/ALT_BOOT -> unconnected-(P5-Pad20)
- P5 pad 21: /Expander, M.2 and T-USB/PWRBTN -> unconnected-(P5-Pad21)
- P5 pad 26: Net-(D10-Pad2) -> /Expander, M.2 and T-USB/VSOM_TU
- P5 pad 34: unconnected-(P5-Pad34) -> /Expander, M.2 and T-USB/FLASH_HOLD
- P5 pad 37: unconnected-(P5-Pad37) -> /Expander, M.2 and T-USB/POWER_PD_CTL_INT
- P5 pad 39: unconnected-(P5-Pad39) -> /Expander, M.2 and T-USB/PD_HRESET
- P5 pad 40: CAM_3V3 -> /Expander, M.2 and T-USB/3V3_TU
- P5 pad 43: CAM_3V3 -> /Expander, M.2 and T-USB/3V3_TU
- P5 pad 46: HDMI_5V -> /Expander, M.2 and T-USB/5V_TU
- P5 pad 49: /Expander, M.2 and T-USB/VCC_RTC -> /Expander, M.2 and T-USB/VCC_RTC_TU
- P6 pad 1: Net-(D7-Pad2) -> /Expander, M.2 and T-USB/VSOM_TU
- P6 pad 16: unconnected-(P6-Pad16) -> GND
- P6 pad 23: unconnected-(P6-Pad23) -> GND
- P6 pad 26: /Expander, M.2 and T-USB/VSOM -> /Expander, M.2 and T-USB/VSOM_TU
- P6 pad 36: Net-(D5-Pad2) -> /Expander, M.2 and T-USB/VSOM_TU
- P6 pad 39: Net-(D4-Pad2) -> /Expander, M.2 and T-USB/VSOM_TU
- P6 pad 42: Net-(D3-Pad2) -> /Expander, M.2 and T-USB/VSOM_TU
- P6 pad 45: Net-(D2-Pad2) -> /Expander, M.2 and T-USB/VSOM_TU
- P6 pad 48: Net-(D1-Pad2) -> /Expander, M.2 and T-USB/VSOM_TU
- P7 pad 24: CAM_3V3 -> SLEEP_3V3
- P7 pad 6: CAM_3V3 -> SLEEP_3V3
- U1 pad 11: /C_FW_TXD -> /C_EX_TXD
- U1 pad 12: /C_FW_RXD -> /C_EX_RXD
- U1 pad 13: /C_SBWTDIO -> /I2C6_SDA
- U1 pad 14: /C_SBWTCK -> /I2C6_SCL
- U1 pad 15: /FACE_FW_TXD -> /F_EX_TXD
- U1 pad 16: /FACE_FW_RXD -> /F_EX_RXD
- U1 pad 17: /FACE_SBWTDIO -> /I2C5_SDA
- U1 pad 18: /FACE_SBWTCK -> /I2C5_SCL
- U1 pad 2: /I2C5_SCL -> /F_SBWTCK
- U1 pad 20: CAM_3V3 -> SLEEP_3V3
- U1 pad 3: /I2C5_SDA -> /F_SBWTDIO
- U1 pad 4: /C_EX_RXD -> /F_FW_RXD
- U1 pad 5: /UART1_RXD -> /F_FW_TXD
- U1 pad 6: /I2C6_SCL -> /C_SBWTCK
- U1 pad 7: /I2C6_SDA -> /C_SBWTDIO
- U1 pad 8: /C_EX_RXD -> /C_FW_RXD
- U1 pad 9: /UART1_RXD -> /C_FW_TXD
- U12 pad 37: /Expander, M.2 and T-USB/POWER_TO_SYS_STEM -> unconnected-(U12-Pad37)
- U12 pad 41: /Expander, M.2 and T-USB/IMU_INTA -> unconnected-(U12-Pad41)
- U12 pad 42: /Expander, M.2 and T-USB/IMU_INTM -> unconnected-(U12-Pad42)
- U19 pad 1: CAM_3V3 -> SLEEP_3V3
- U2 pad 14: CAM_3V3 -> SLEEP_3V3
- U20 pad 1: CAM_3V3 -> SLEEP_3V3
- U21 pad 1: CAM_3V3 -> SLEEP_3V3
- U4 pad 1: CAM_3V3 -> SLEEP_3V3
- U4 pad 2: CAM_3V3 -> SLEEP_3V3
- U7 pad 13: /Expander, M.2 and T-USB/SYS_EX_nINT -> /Expander, M.2 and T-USB/PD_USBC_INT
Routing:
- net +VDC: track 112.9 -> 0.00 mm
- net (no net): track 1574.7 -> 1687.6 mm
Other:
- outline, holes or cut-outs redrawn
